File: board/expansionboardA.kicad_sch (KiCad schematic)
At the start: 61 parts, among them J2 USB_A_Stacked, J3 HDMI_A, J4 FAN, P1 USB_C_Plug, U1 MAX3420EECJ, U2 GPIO_U2, U4 GPIO_U4, U5 MCP3008T-I/SL, U6 CS4344-CZZR, U7 MAX3421EEHJ+T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

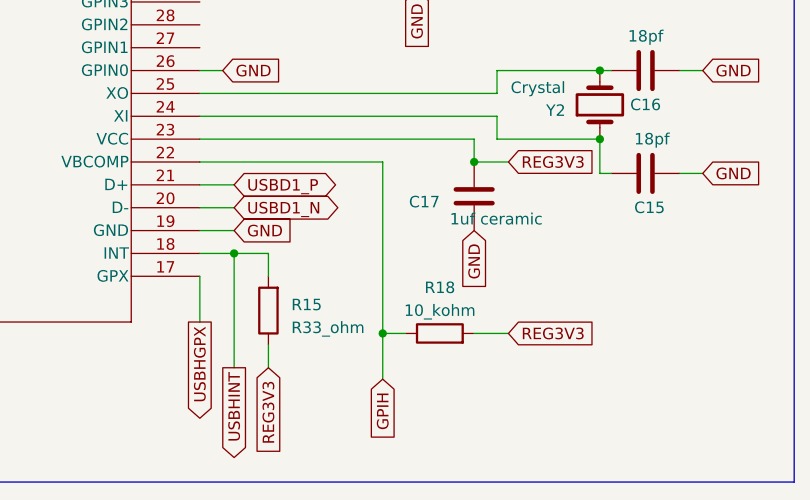
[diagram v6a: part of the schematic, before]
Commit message: Final board design for issue 1J Working on USB host - HID support
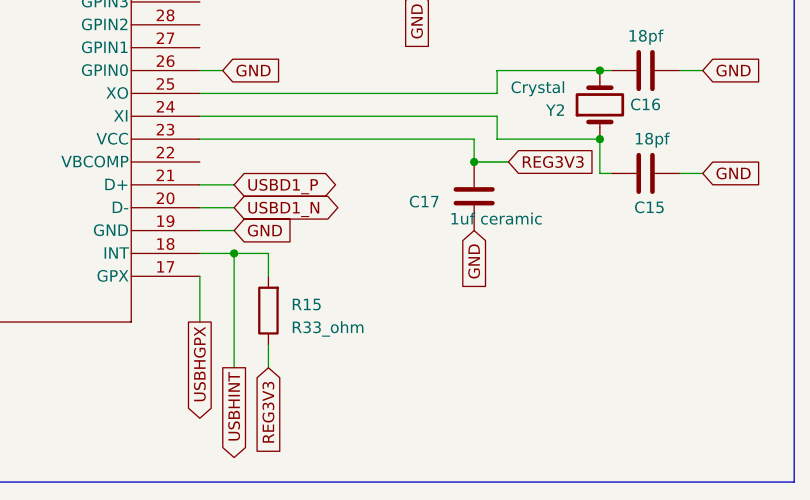
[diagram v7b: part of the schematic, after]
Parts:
- removed R18: 10_kohm, Resistor_SMD:R_0603_1608Metric_Pad0.98x0.95mm_HandSolder, symbol Device:R
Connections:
- net GPIH: no longer names the net of U7.22 (VBCOMP)
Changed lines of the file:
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@@
   (junction (at 322.58 97.79) (diameter 0) (color 0 0 0 0)
   )
-  (junction (at 224.79 236.22) (diameter 0) (color 0 0 0 0)
-  )
   (junction (at 374.65 204.47) (diameter 0) (color 0 0 0 0)
   )
@@
     (stroke (width 0) (type default))
   )
-  (wire (pts (xy 224.79 241.3) (xy 224.79 236.22))
-    (stroke (width 0) (type default))
-  )
   (wire (pts (xy 316.23 113.03) (xy 316.23 115.57))
     (stroke (width 0) (type default))
@@
     (stroke (width 0) (type default))
   )
-  (wire (pts (xy 204.47 217.17) (xy 224.79 217.17))
-    (stroke (width 0) (type default))
-  )
   (wire (pts (xy 359.41 92.71) (xy 370.84 92.71))
     (stroke (width 0) (type default))
@@
     (stroke (width 0) (type default))
   )
-  (wire (pts (xy 224.79 217.17) (xy 224.79 236.22))
-    (stroke (width 0) (type default))
-  )
   (wire (pts (xy 219.71 129.54) (xy 215.9 129.54))
     (stroke (width 0) (type default))
@@
     (stroke (width 0) (type default))
   )
-  (wire (pts (xy 224.79 236.22) (xy 227.33 236.22))
-    (stroke (width 0) (type default))
-  )
   (wire (pts (xy 316.23 115.57) (xy 323.85 115.57))
     (stroke (width 0) (type default))
@@
     (stroke (width 0) (type default))
   )
-  (wire (pts (xy 234.95 236.22) (xy 238.76 236.22))
-    (stroke (width 0) (type default))
-  )
   (wire (pts (xy 149.86 158.75) (xy 152.4 158.75))
     (stroke (width 0) (type default))
@@
     )
   )
-  (global_label "GPIH" (shape input) (at 224.79 241.3 270) (fields_autoplaced)
-    (effects (font (size 1.27 1.27)) (justify right))
-    (property "Intersheetrefs" "${INTERSHEET_REFS}" (at 224.79 248.6811 90)
-      (effects (font (size 1.27 1.27)) (justify right) hide)
-    )
-  )
   (global_label "USBD1_P" (shape bidirectional) (at 208.28 219.71 0) (fields_autoplaced)
     (effects (font (size 1.27 1.27)) (justify left))
@@
     )
   )
-  (global_label "REG3V3" (shape input) (at 238.76 236.22 0) (fields_autoplaced)
-    (effects (font (size 1.27 1.27)) (justify left))
-    (property "Intersheetrefs" "${INTERSHEET_REFS}" (at 248.8624 236.22 0)
-      (effects (font (size 1.27 1.27)) (justify left) hide)
-    )
-  )
   (global_label "ADCH4" (shape input) (at 147.32 110.49 270) (fields_autoplaced)
     (effects (font (size 1.27 1.27)) (justify right))
@@
         )
       )
-    )
-  )
-  (symbol (lib_id "Device:R") (at 231.14 236.22 90) (unit 1)
-    (in_bom yes) (on_board yes) (dnp no) (fields_autoplaced)
-    (property "Reference" "R18" (at 231.14 231.14 90)
-      (effects (font (size 1.27 1.27)))
-    )
-    (property "Value" "10_kohm" (at 231.14 233.68 90)
-      (effects (font (size 1.27 1.27)))
-    )
-    (property "Footprint" "Resistor_SMD:R_0603_1608Metric_Pad0.98x0.95mm_HandSolder" (at 231.14 237.998 90)
-      (effects (font (size 1.27 1.27)) hide)
-    )
-    (property "Datasheet" "~" (at 231.14 236.22 0)
-      (effects (font (size 1.27 1.27)) hide)
-    )
-    (pin "1")
-    (pin "2")
-    (instances
-      (project "expansionboardA"
-        (path "/317f7f3e-4535-46d0-9a87-af1bea12706a"
-          (reference "R18") (unit 1)
-        )
-      )

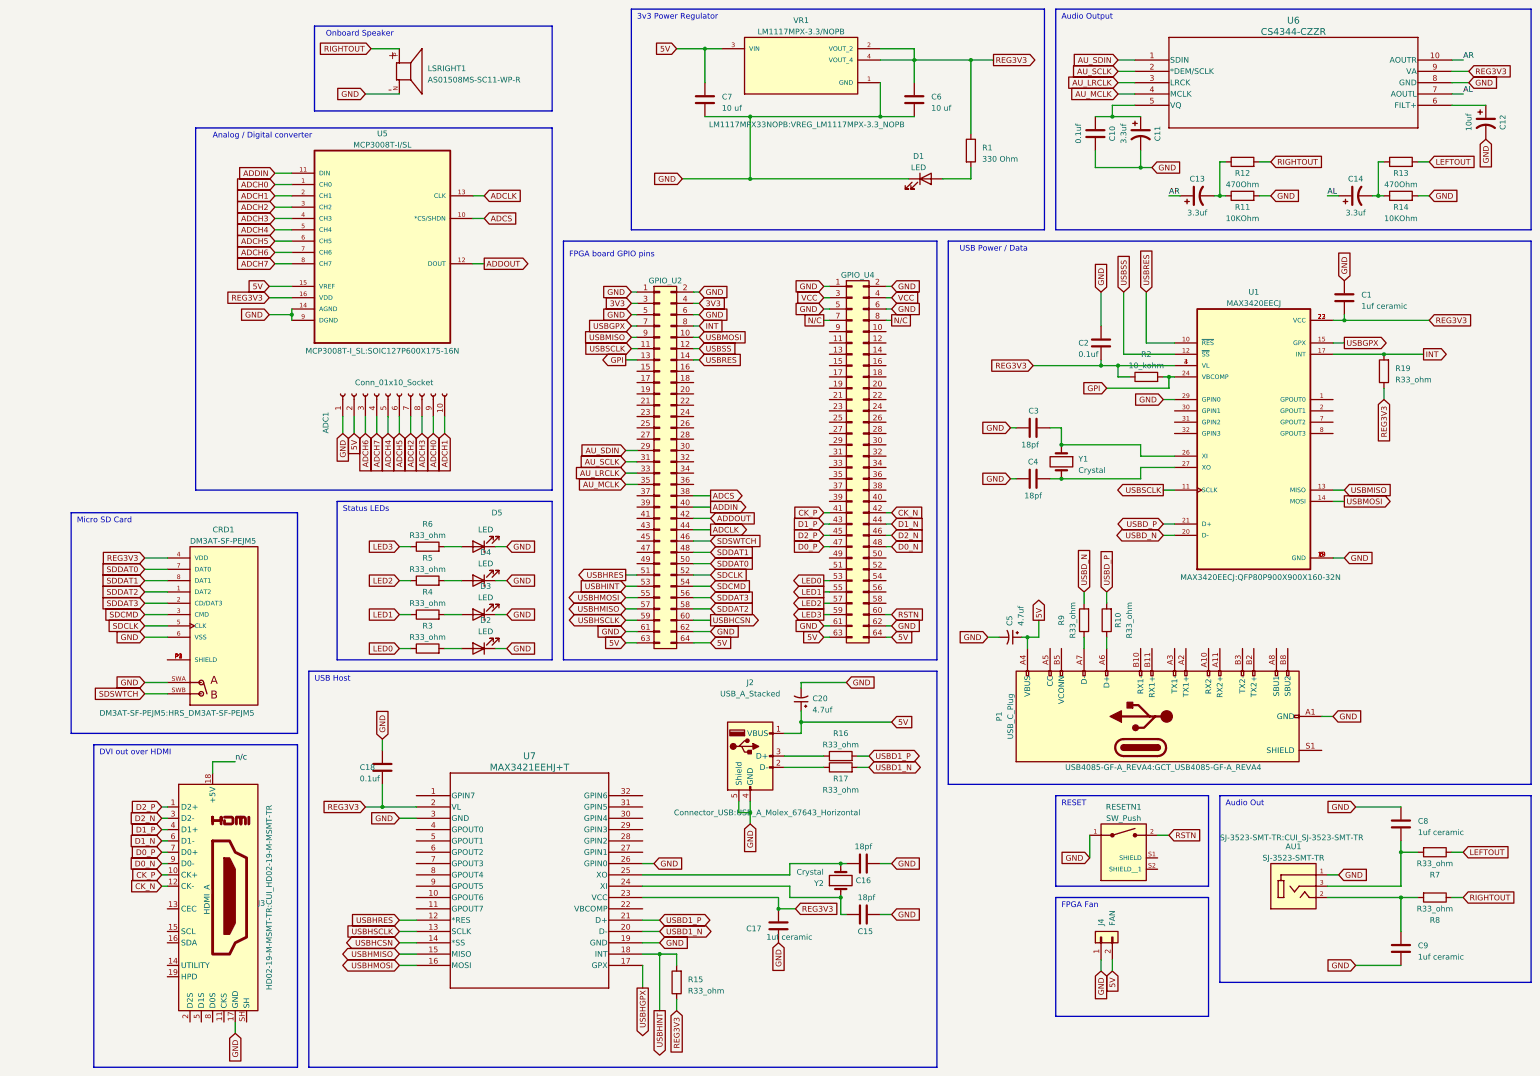
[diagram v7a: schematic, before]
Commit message: minor fixes to usbenum added string usbenum increased poll interval to 20ms
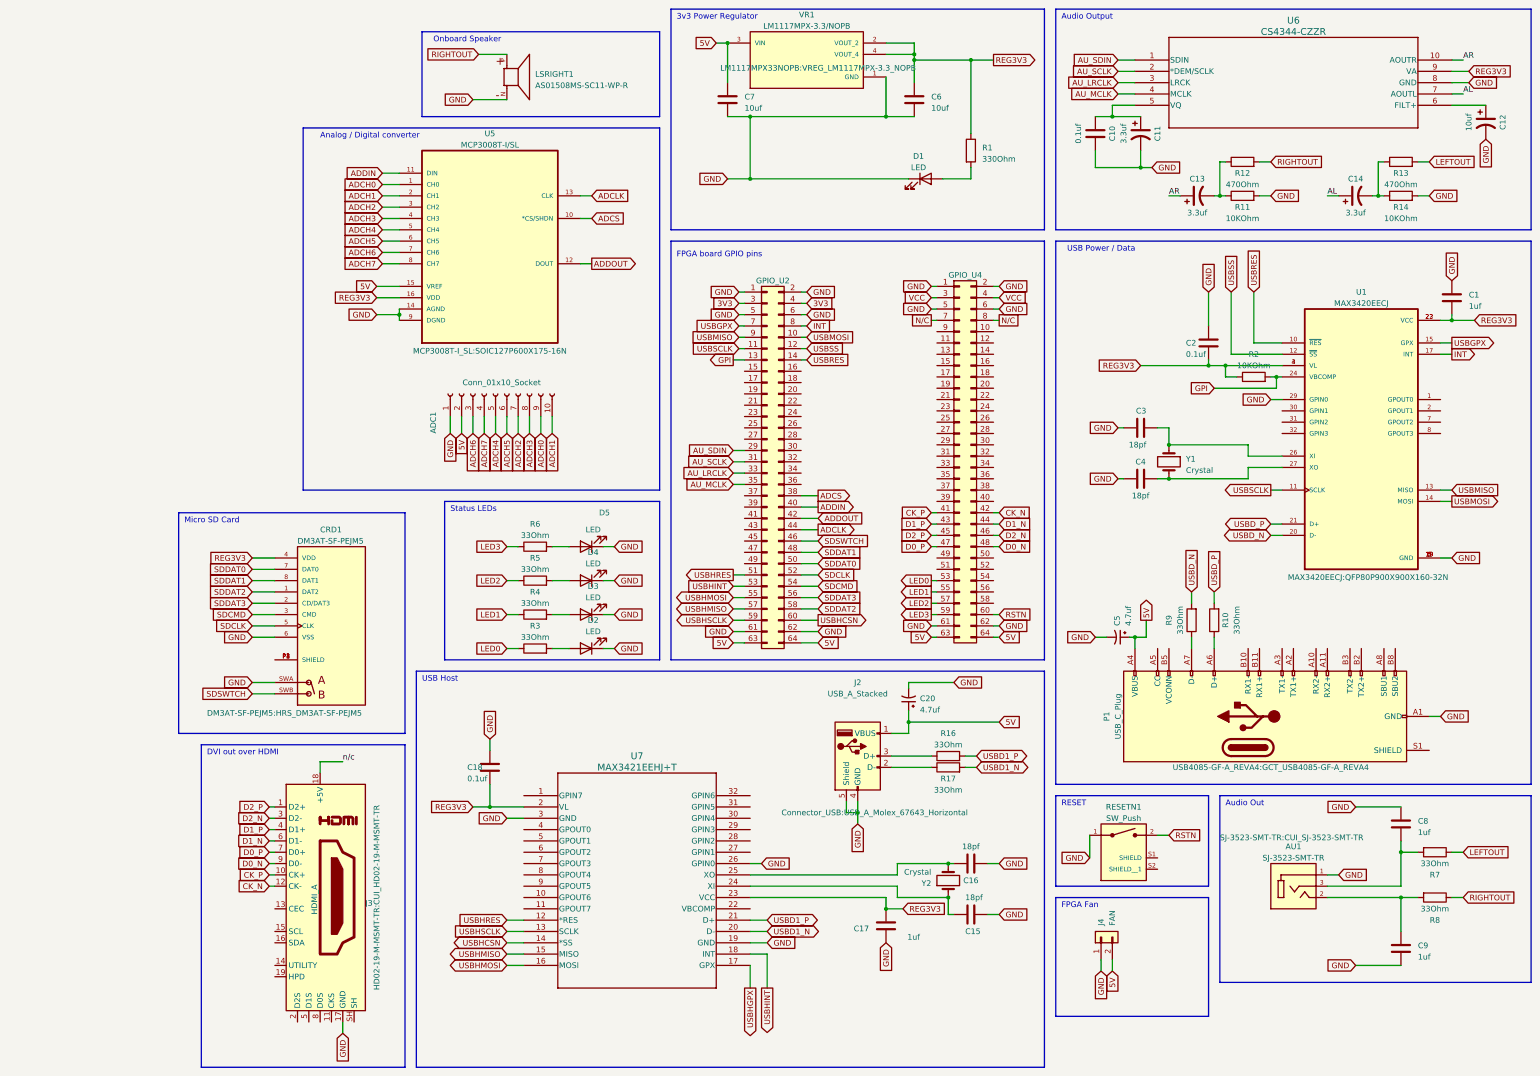
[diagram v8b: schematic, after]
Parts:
- removed R15, R19: R33_ohm, Resistor_SMD:R_0603_1608Metric_Pad0.98x0.95mm_HandSolder, symbol Device:R
- C1, C17, C8, C9: value 1uf ceramic -> 1uf
- C6, C7: value 10 uf -> 10uf
- R1: value 330 Ohm -> 330Ohm
- R10, R16, R17, R3, R4, R5, R6, R7, R8, R9: value R33_ohm -> 33Ohm
- R2: value 10_kohm -> 10KOhm
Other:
- moved on the sheet: ADC1, C1, C15, C16, C17, C18, C2, C20, C3, C4, C5, C7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
